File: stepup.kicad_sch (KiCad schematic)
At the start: 13 parts, among them J1 USB plug, J2 Conn_01x02_Socket, U1 MC33063AP

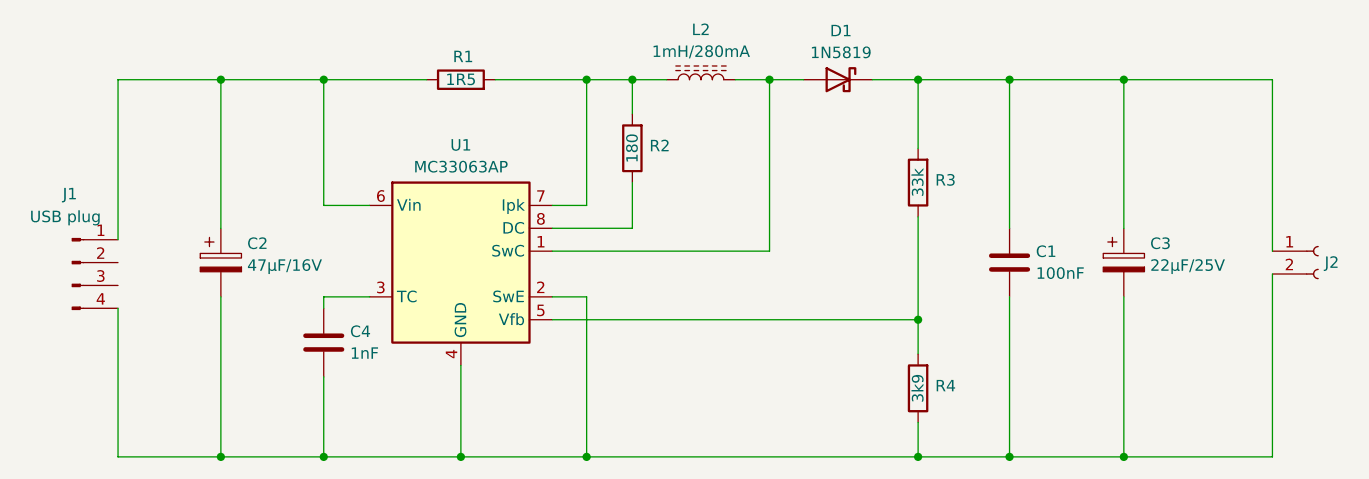
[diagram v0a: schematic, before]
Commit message: component values and footprints updated
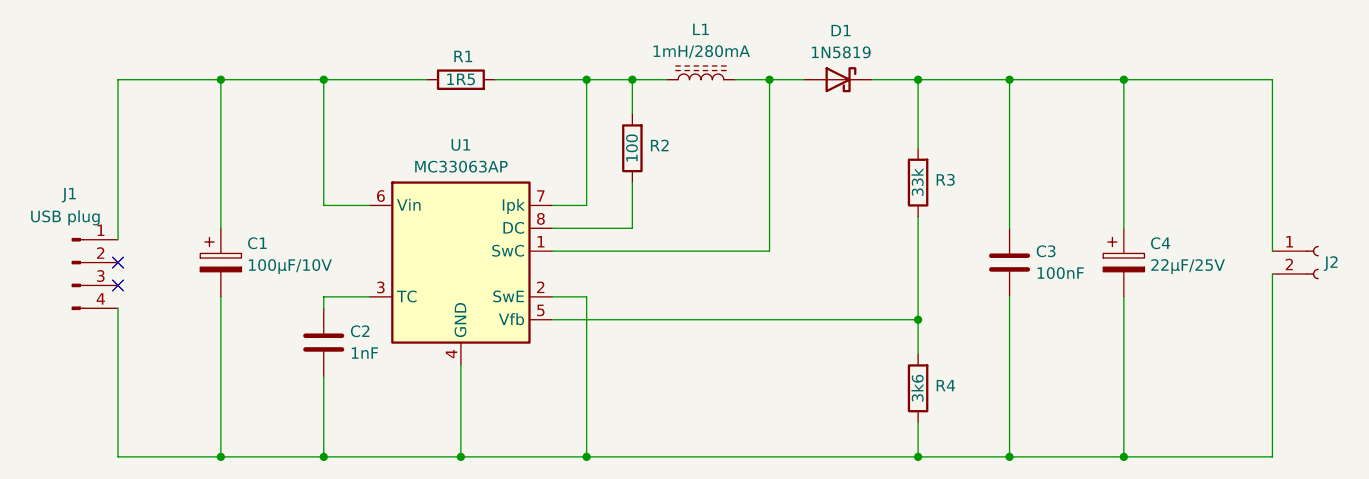
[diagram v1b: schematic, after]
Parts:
- C1: renamed from C2; value 47μF/16V -> 100μF/10V; footprint (none) -> Capacitor_THT:CP_Radial_D5.0mm_P2.50mm
- C2: renamed from C4; footprint (none) -> Capacitor_THT:C_Rect_L7.0mm_W3.5mm_P5.00mm
- C3: renamed from C1; footprint (none) -> Capacitor_THT:C_Rect_L7.0mm_W3.5mm_P5.00mm
- C4: renamed from C3; footprint (none) -> Capacitor_THT:CP_Radial_D8.0mm_P3.80mm
- J1: footprint (none) -> Connector_PinHeader_2.54mm:PinHeader_1x04_P2.54mm_Vertical
- J2: footprint (none) -> Connector_PinHeader_2.54mm:PinHeader_1x02_P2.54mm_Vertical
- L1: renamed from L2; footprint (none) -> Inductor_THT:L_Radial_D8.7mm_P5.00mm_Fastron_07HCP
- R1, R3: footprint (none) -> Resistor_THT:R_Axial_DIN0309_L9.0mm_D3.2mm_P2.54mm_Vertical
- R2: value 180 -> 100; footprint (none) -> Resistor_THT:R_Axial_DIN0309_L9.0mm_D3.2mm_P2.54mm_Vertical
- R4: value 3k9 -> 3k6; footprint (none) -> Resistor_THT:R_Axial_DIN0309_L9.0mm_D3.2mm_P2.54mm_Vertical
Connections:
- no-connect marks 0 -> 2
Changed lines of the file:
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@@
 		(color 0 0 0 0)
+	)
+	(no_connect
+		(at 82.55 93.98)
+	)
+	(no_connect
+		(at 82.55 91.44)
 	)
 	(wire
@@
 			)
 		)
-		(property "Value" "180"
+		(property "Value" "100"
 			(at 139.7 78.74 90)
 			(effects
@@
 			)
 		)
-		(property "Footprint" ""
+		(property "Footprint" "Resistor_THT:R_Axial_DIN0309_L9.0mm_D3.2mm_P2.54mm_Vertical"
 			(at 141.478 78.74 90)
 			(effects
@@
 			)
 		)
-		(property "Footprint" ""
+		(property "Footprint" "Resistor_THT:R_Axial_DIN0309_L9.0mm_D3.2mm_P2.54mm_Vertical"
 			(at 173.228 82.55 90)
 			(effects
@@
 			)
 		)
-		(property "Footprint" ""
+		(property "Footprint" "Connector_PinHeader_2.54mm:PinHeader_1x04_P2.54mm_Vertical"
 			(at 77.47 91.44 0)
 			(effects
@@
 			)
 		)
-		(property "Footprint" ""
+		(property "Footprint" "Resistor_THT:R_Axial_DIN0309_L9.0mm_D3.2mm_P2.54mm_Vertical"
 			(at 120.65 72.898 90)
 			(effects
@@
 		(dnp no)
 		(fields_autoplaced yes)
-		(property "Reference" "C1"
+		(property "Reference" "C3"
 			(at 184.531 90.2278 0)
 			(effects
@@
 			)
 		)
-		(property "Footprint" ""
+		(property "Footprint" "Capacitor_THT:C_Rect_L7.0mm_W3.5mm_P5.00mm"
 			(at 182.5752 95.25 0)
 			(effects
@@
 			(project ""
 				(path "/12565e44-deac-4949-8d6f-9da5b7013c32"
-					(reference "C1")
+					(reference "C3")
 					(unit 1)
 				)
@@
 		(dnp no)
 		(fields_autoplaced yes)
-		(property "Reference" "C2"
+		(property "Reference" "C1"
 			(at 96.901 89.3388 0)
 			(effects
@@
 			)
 		)
-		(property "Value" "47μF/16V"
+		(property "Value" "100μF/10V"
 			(at 96.901 91.7631 0)
 			(effects
@@
 			)
 		)
-		(property "Footprint" ""
+		(property "Footprint" "Capacitor_THT:CP_Radial_D5.0mm_P2.50mm"
 			(at 94.9452 95.25 0)
 			(effects
@@
 			(project ""
 				(path "/12565e44-deac-4949-8d6f-9da5b7013c32"
-					(reference "C2")
+					(reference "C1")
 					(unit 1)
 				)
@@
 			)
 		)
-		(property "Value" "3k9"
+		(property "Value" "3k6"
 			(at 171.45 105.41 90)
 			(effects
@@
 			)
 		)
-		(property "Footprint" ""
+		(property "Footprint" "Resistor_THT:R_Axial_DIN0309_L9.0mm_D3.2mm_P2.54mm_Vertical"
 			(at 173.228 105.41 90)
 			(effects
@@
 		(dnp no)
 		(fields_autoplaced yes)
-		(property "Reference" "C4"
+		(property "Reference" "C2"
 			(at 108.331 99.1178 0)
 			(effects
@@
 			)
 		)
-		(property "Footprint" ""
+		(property "Footprint" "Capacitor_THT:C_Rect_L7.0mm_W3.5mm_P5.00mm"
 			(at 106.3752 104.14 0)
 			(effects
@@
 			(project "stepup"
 				(path "/12565e44-deac-4949-8d6f-9da5b7013c32"
-					(reference "C4")
+					(reference "C2")
 					(unit 1)
 				)
@@
 		(dnp no)
 		(fields_autoplaced yes)
-		(property "Reference" "C3"
+		(property "Reference" "C4"
 			(at 197.231 89.3388 0)
 			(effects
@@
 			)
 		)
-		(property "Footprint" ""
+		(property "Footprint" "Capacitor_THT:CP_Radial_D8.0mm_P3.80mm"
 			(at 195.2752 95.25 0)
 			(effects
@@
 			(project "stepup"
 				(path "/12565e44-deac-4949-8d6f-9da5b7013c32"
-					(reference "C3")
+					(reference "C4")
 					(unit 1)
 				)
@@
 			)
 		)
-		(property "Footprint" ""
+		(property "Footprint" "Connector_PinHeader_2.54mm:PinHeader_1x02_P2.54mm_Vertical"
 			(at 215.9 90.17 0)
 			(effects
@@
 		(dnp no)
 		(fields_autoplaced yes)
-		(property "Reference" "L2"
+		(property "Reference" "L1"
 			(at 147.32 65.5785 90)
 			(effects
@@
 			)
 		)
-		(property "Footprint" ""
+		(property "Footprint" "Inductor_THT:L_Radial_D8.7mm_P5.00mm_Fastron_07HCP"
 			(at 147.32 71.12 0)
 			(effects
@@
 			(project ""
 				(path "/12565e44-deac-4949-8d6f-9da5b7013c32"
-					(reference "L2")
+					(reference "L1")
 					(unit 1)
 				)
